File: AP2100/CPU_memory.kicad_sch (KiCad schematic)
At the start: 1 part, among them U3 LS1043ASE7KQB

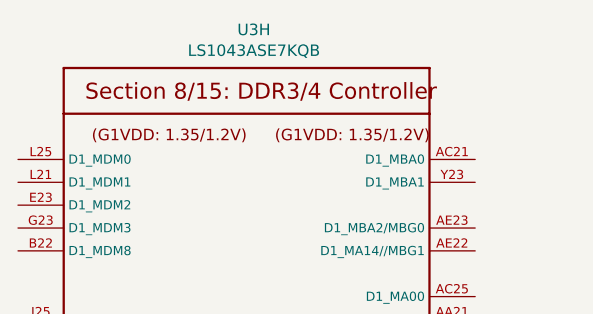
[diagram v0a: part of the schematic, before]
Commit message: Add PartsBox part numbers to everything so far
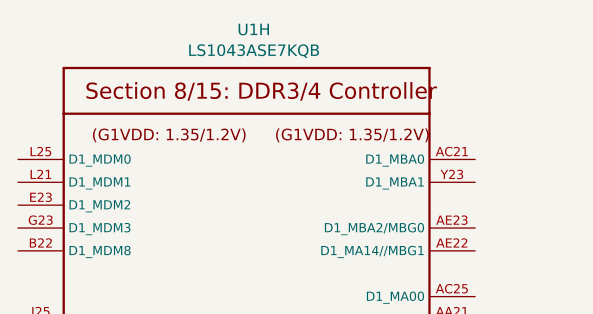
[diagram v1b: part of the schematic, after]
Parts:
- U1: renamed from U3; PartsBoxID (none) -> LS1043ASE7MNLB
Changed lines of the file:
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@@
   (symbol (lib_id "AP2100-rescue:LS1043ASE7KQB-Layerscape") (at 72.39 100.33 0) (unit 8)
     (in_bom yes) (on_board yes)
-    (property "Reference" "U3" (id 0) (at 71.9328 17.3482 0))
+    (property "Reference" "U1" (id 0) (at 71.9328 17.3482 0))
     (property "Value" "LS1043ASE7KQB" (id 1) (at 71.9328 19.6596 0))
     (property "Footprint" "PLS1043ASE7QQA:BGA621C80P25X25_2100X2100X192N" (id 2) (at 72.39 100.33 0)
@@
       (effects (font (size 1.27 1.27)) hide)
     )
+    (property "PartsBoxID" "LS1043ASE7MNLB" (id 4) (at 72.39 100.33 0)
+      (effects (font (size 1.27 1.27)) hide)
+    )

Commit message: More work on memory
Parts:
- added C? (x4): 1uF, Capacitor_SMD:C_0402_1005Metric, symbol Device:C_Small
- added C? (x16): .1uF, Capacitor_SMD:C_0402_1005Metric, symbol Device:C_Small
- added C? (x4): 10uF, Capacitor_SMD:C_0805_2012Metric, symbol Device:C_Small
- added IC3, IC4: AS4C256M16D4-75BCN, Scott:BGA96C80P9X16_750X1350X120, symbol Scott:AS4C256M16D4
- U1: MFR - -> (none)
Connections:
- new net +GVDD: C?.1, C?.1, C?.1, C?.1, C?.1, C?.1, C?.1, C?.1, C?.1, C?.1, C?.1, C?.1, C?.1, C?.1, C?.1, C?.1, C?.1, C?.1, C?.1, C?.1, IC3.A1 (VDDQ_1), IC3.A9 (VDDQ_2), IC3.B3 (VDD_1), IC3.B9 (VDD_2), IC3.C1 (VDDQ_3), IC3.D1 (VDD_3), IC3.D9 (VDDQ_4), IC3.F2 (VDDQ_5), IC3.F8 (VDDQ_6), IC3.G1 (VDDQ_7), IC3.G7 (VDD_4), IC3.G9 (VDDQ_8), IC3.J1 (VDD_5), IC3.J2 (VDDQ_9), IC3.J8 (VDDQ_10), IC3.J9 (VDD_6), IC3.L1 (VDD_7), IC3.L9 (VDD_8), IC3.R1 (VDD_9), IC3.T9 (VDD_10), IC4.A1 (VDDQ_1), IC4.A9 (VDDQ_2), IC4.B3 (VDD_1), IC4.B9 (VDD_2), IC4.C1 (VDDQ_3), IC4.D1 (VDD_3), IC4.D9 (VDDQ_4), IC4.F2 (VDDQ_5), IC4.F8 (VDDQ_6), IC4.G1 (VDDQ_7), IC4.G7 (VDD_4), IC4.G9 (VDDQ_8), IC4.J1 (VDD_5), IC4.J2 (VDDQ_9), IC4.J8 (VDDQ_10), IC4.J9 (VDD_6), IC4.L1 (VDD_7), IC4.L9 (VDD_8), IC4.R1 (VDD_9), IC4.T9 (VDD_10)
- new net 2V5_VPP: C?.1, C?.1, C?.1, C?.1, IC3.B1 (VPP_1), IC3.R9 (VPP_2), IC4.B1 (VPP_1), IC4.R9 (VPP_2)
- new net GND: C?.2, C?.2, C?.2, C?.2, C?.2, C?.2, C?.2, C?.2, C?.2, C?.2, C?.2, C?.2, C?.2, C?.2, C?.2, C?.2, C?.2, C?.2, C?.2, C?.2, C?.2, C?.2, C?.2, C?.2, IC3.A2 (VSSQ_1), IC3.A8 (VSSQ_2), IC3.B2 (VSS_1), IC3.C9 (VSSQ_3), IC3.D2 (VSSQ_4), IC3.D8 (VSSQ_5), IC3.E1 (VSS_2), IC3.E3 (VSSQ_6), IC3.E8 (VSSQ_7), IC3.E9 (VSS_3), IC3.F1 (VSSQ_8), IC3.G8 (VSS_4), IC3.H1 (VSSQ_9), IC3.H9 (VSSQ_10), IC3.K1 (VSS_5), IC3.K9 (VSS_6), IC3.M9 (VSS_7), IC3.N1 (VSS_8), IC3.T1 (VSS_9), IC4.A2 (VSSQ_1), IC4.A8 (VSSQ_2), IC4.B2 (VSS_1), IC4.C9 (VSSQ_3), IC4.D2 (VSSQ_4), IC4.D8 (VSSQ_5), IC4.E1 (VSS_2), IC4.E3 (VSSQ_6), IC4.E8 (VSSQ_7), IC4.E9 (VSS_3), IC4.F1 (VSSQ_8), IC4.G8 (VSS_4), IC4.H1 (VSSQ_9), IC4.H9 (VSSQ_10), IC4.K1 (VSS_5), IC4.K9 (VSS_6), IC4.M9 (VSS_7), IC4.N1 (VSS_8), IC4.T1 (VSS_9)
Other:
- moved on the sheet: U1H

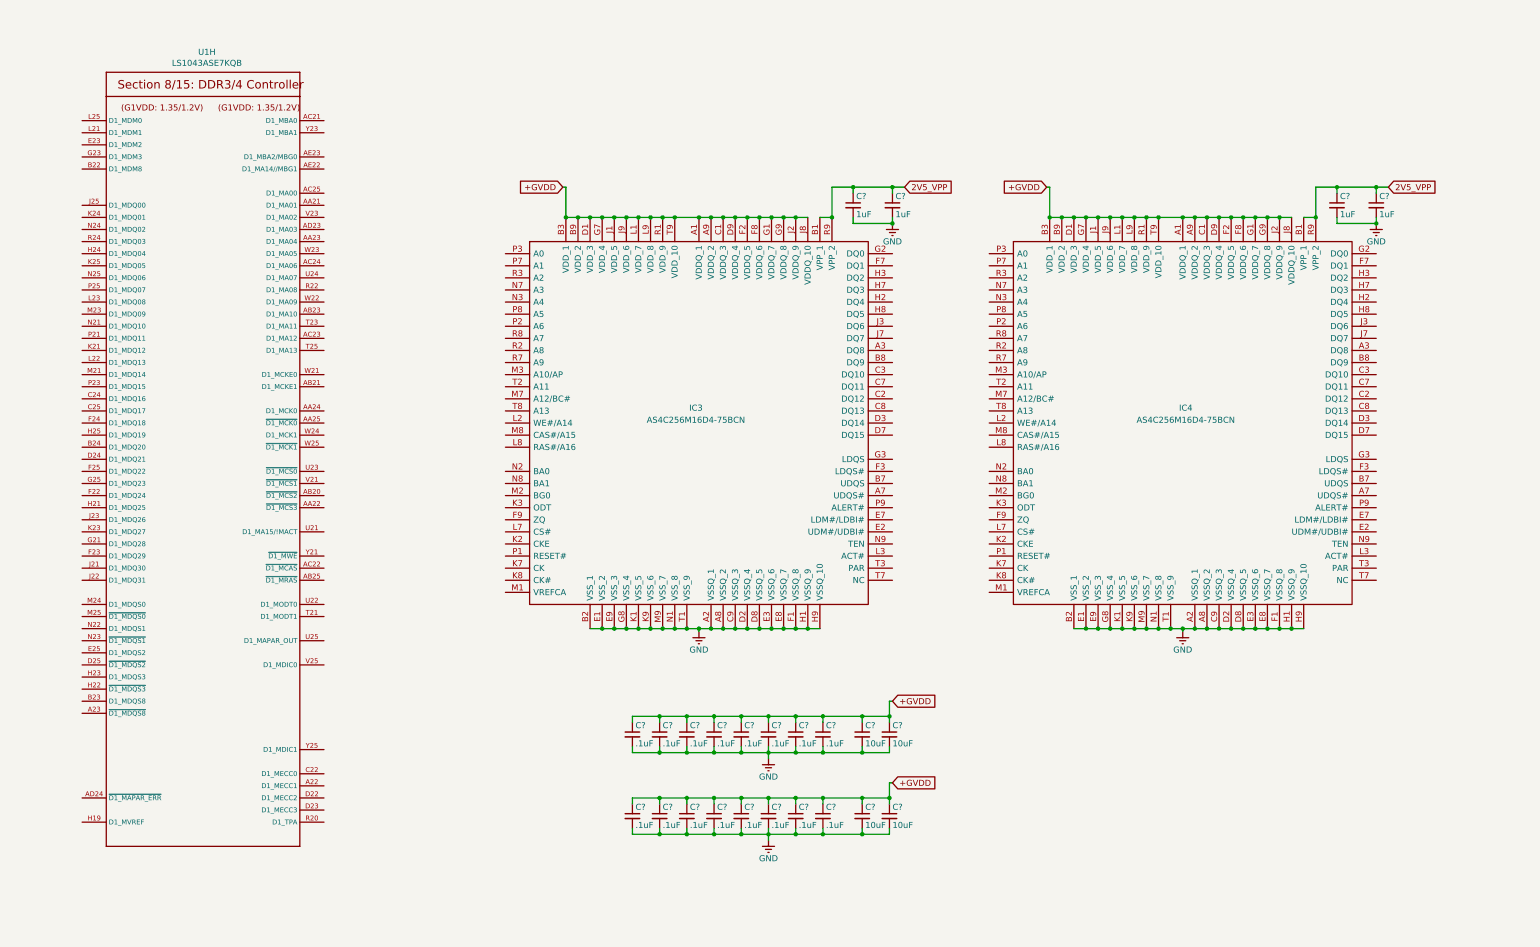
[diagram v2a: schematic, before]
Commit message: Add + route first 16 memory data lines
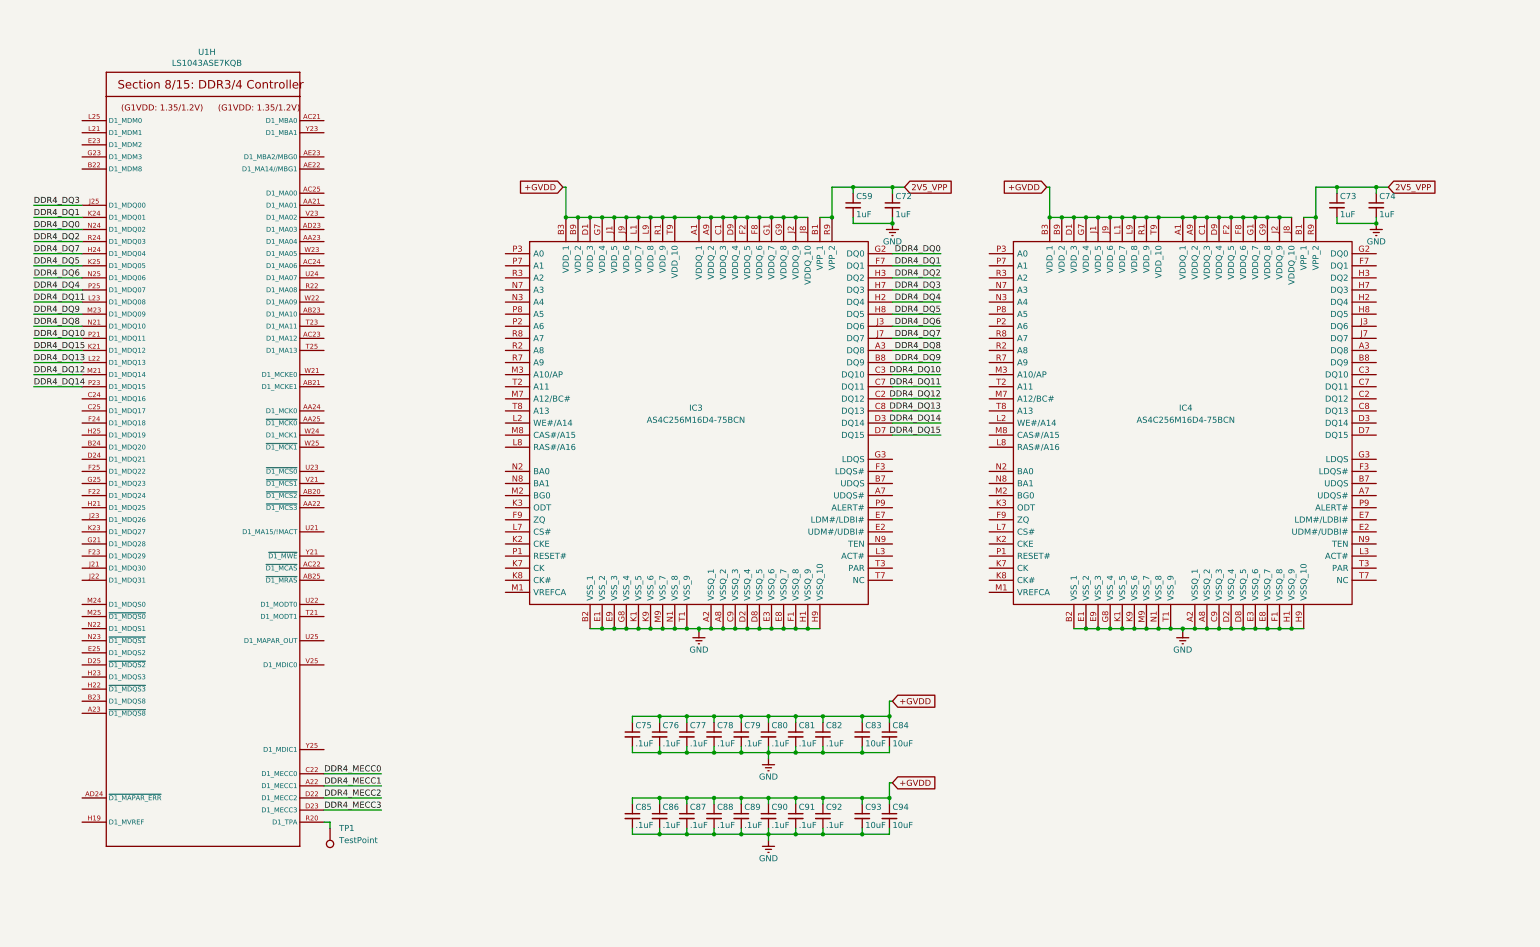
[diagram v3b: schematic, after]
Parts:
- added TP1: TestPoint, symbol Connector:TestPoint
- gave numbers to parts that had none: 24
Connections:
- net DDR4_MECC1: now reaches U1.A22 (D1_MECC1)
- net DDR4_MECC0: now reaches U1.C22 (D1_MECC0)
- net DDR4_MECC2: now reaches U1.D22 (D1_MECC2)
- net DDR4_MECC3: now reaches U1.D23 (D1_MECC3)
- net DDR4_DQ7: now reaches U1.H24 (D1_MDQ04)
- net DDR4_DQ7: now also IC3.J7 (DQ7)
- net DDR4_DQ3: now reaches U1.J25 (D1_MDQ00)
- net DDR4_DQ3: now also IC3.H7 (DQ3)
- net DDR4_DQ15: now reaches U1.K21 (D1_MDQ12)
- net DDR4_DQ15: now also IC3.D7 (DQ15)
- net DDR4_DQ1: now reaches U1.K24 (D1_MDQ01)
- net DDR4_DQ1: now also IC3.F7 (DQ1)
- net DDR4_DQ5: now reaches U1.K25 (D1_MDQ05)
- net DDR4_DQ5: now also IC3.H8 (DQ5)
- net DDR4_DQ13: now reaches U1.L22 (D1_MDQ13)
- net DDR4_DQ13: now also IC3.C8 (DQ13)
- net DDR4_DQ11: now reaches U1.L23 (D1_MDQ08)
- net DDR4_DQ11: now also IC3.C7 (DQ11)
- net DDR4_DQ12: now reaches U1.M21 (D1_MDQ14)
- net DDR4_DQ12: now also IC3.C2 (DQ12)
- net DDR4_DQ9: now reaches U1.M23 (D1_MDQ09)
- net DDR4_DQ9: now also IC3.B8 (DQ9)
- net DDR4_DQ8: now reaches U1.N21 (D1_MDQ10)
- net DDR4_DQ8: now also IC3.A3 (DQ8)
- net DDR4_DQ0: now reaches U1.N24 (D1_MDQ02)
- net DDR4_DQ0: now also IC3.G2 (DQ0)
- net DDR4_DQ6: now reaches U1.N25 (D1_MDQ06)
- net DDR4_DQ6: now also IC3.J3 (DQ6)
- net DDR4_DQ10: now reaches U1.P21 (D1_MDQ11)
- net DDR4_DQ10: now also IC3.C3 (DQ10)
- net DDR4_DQ14: now reaches U1.P23 (D1_MDQ15)
- net DDR4_DQ14: now also IC3.D3 (DQ14)
- net DDR4_DQ4: now reaches U1.P25 (D1_MDQ07)
- net DDR4_DQ4: now also IC3.H2 (DQ4)
- net at U1.R20 (D1_TPA): now also TP1.1
- net DDR4_DQ2: now reaches U1.R24 (D1_MDQ03)
- net DDR4_DQ2: now also IC3.H3 (DQ2)

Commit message: Almost finish memory section
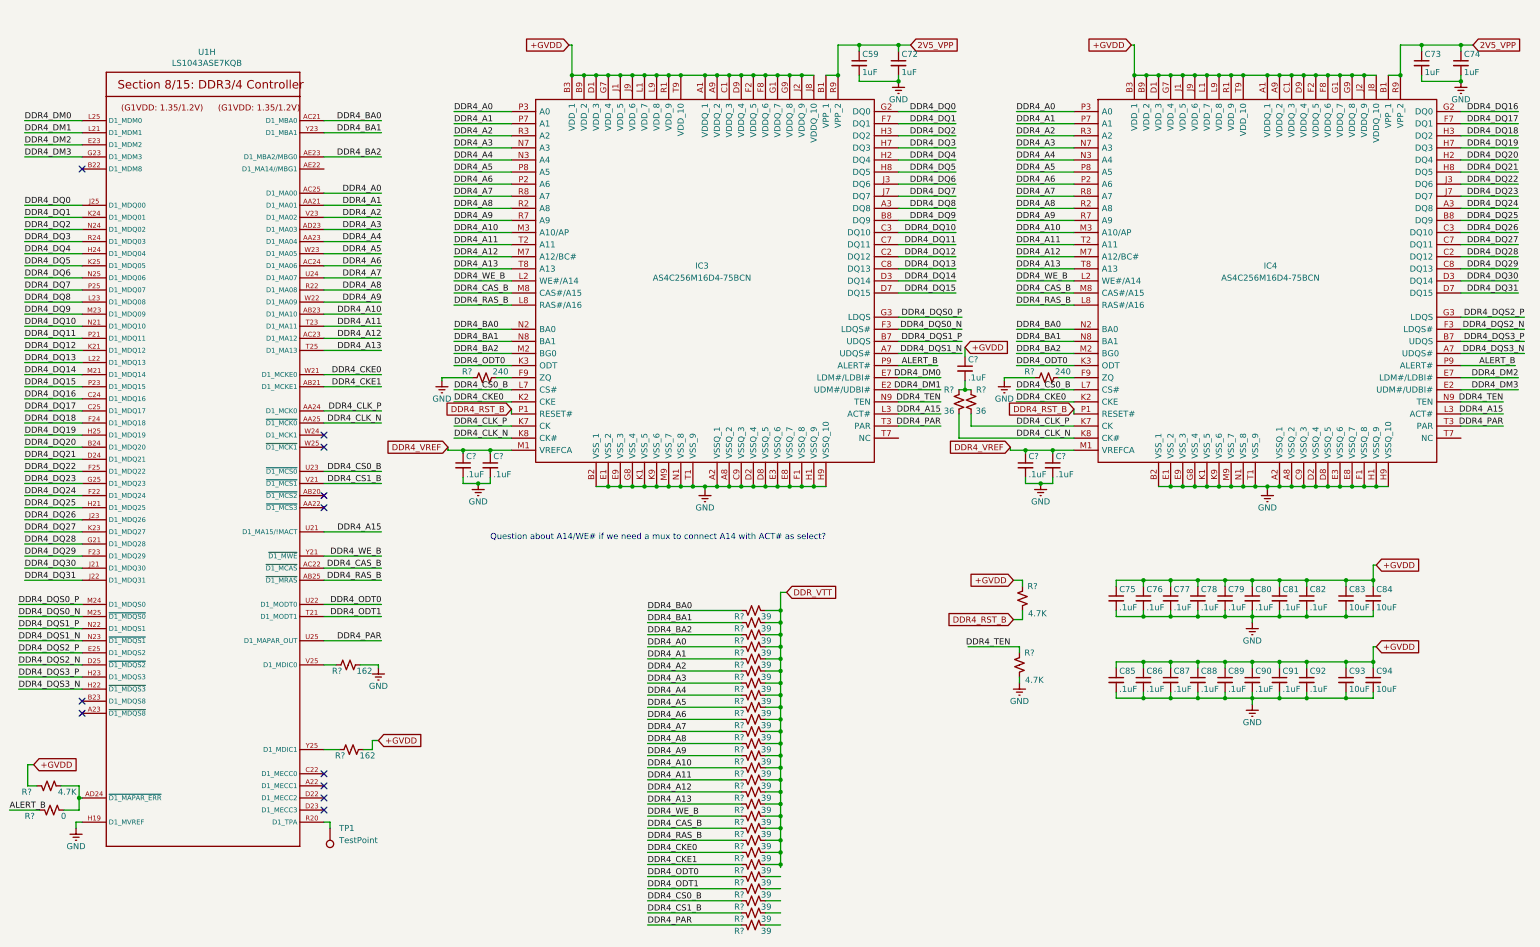
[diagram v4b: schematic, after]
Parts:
- added C? (x5): .1uF, Capacitor_SMD:C_0402_1005Metric, symbol Device:C_Small
- added R? (x27): 39, Resistor_SMD:R_0402_1005Metric, symbol Device:R_Small_US
- added R? (x2): 36, Resistor_SMD:R_0402_1005Metric, symbol Device:R_Small_US
- added R? (x2): 240, Resistor_SMD:R_0402_1005Metric, symbol Device:R_Small_US
- added R? (x3): 4.7K, Resistor_SMD:R_0402_1005Metric, symbol Device:R_Small_US
- added R?: 0, Resistor_SMD:R_0402_1005Metric, symbol Device:R_Small_US
- added R? (x2): 162, Resistor_SMD:R_0402_1005Metric, symbol Device:R_Small_US
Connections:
- net +GVDD: now also C?.1, R?.1, R?.2, R?.2
- net DDR4_DQ0: now also U1.J25 (D1_MDQ00); no longer U1.N24 (D1_MDQ02)
- net DDR4_DQ10: now also U1.N21 (D1_MDQ10); no longer U1.P21 (D1_MDQ11)
- net DDR4_DQ11: now also U1.P21 (D1_MDQ11); no longer U1.L23 (D1_MDQ08)
- net DDR4_DQ12: now also U1.K21 (D1_MDQ12); no longer U1.M21 (D1_MDQ14)
- net DDR4_DQ14: now also U1.M21 (D1_MDQ14); no longer U1.P23 (D1_MDQ15)
- net DDR4_DQ15: now also U1.P23 (D1_MDQ15); no longer U1.K21 (D1_MDQ12)
- net DDR4_DQ2: now also U1.N24 (D1_MDQ02); no longer U1.R24 (D1_MDQ03)
- net DDR4_DQ3: now also U1.R24 (D1_MDQ03); no longer U1.J25 (D1_MDQ00)
- net DDR4_DQ4: now also U1.H24 (D1_MDQ04); no longer U1.P25 (D1_MDQ07)
- net DDR4_DQ7: now also U1.P25 (D1_MDQ07); no longer U1.H24 (D1_MDQ04)
- net DDR4_DQ8: now also U1.L23 (D1_MDQ08); no longer U1.N21 (D1_MDQ10)
- net GND: now also U1.H19 (D1_MVREF), C?.2, C?.2, C?.2, C?.2, R?.1, R?.1, R?.2, R?.2
- net DDR4_A1: now reaches U1.AA21 (D1_MA01)
- net DDR4_A1: now also IC3.P7 (A1), IC4.P7 (A1), R?.1
- net DDR4_A4: now reaches U1.AA23 (D1_MA04)
- net DDR4_A4: now also IC3.N3 (A4), IC4.N3 (A4), R?.1
- net DDR4_CLK_P: now reaches U1.AA24 (D1_MCK0)
- net DDR4_CLK_P: now also IC3.K7 (CK), IC4.K7 (CK), R?.1
- net DDR4_CLK_N: now reaches U1.AA25 (~D1_MCK0~)
- net DDR4_CLK_N: now also IC3.K8 (CK#), IC4.K8 (CK#), R?.1
- net DDR4_CKE1: now reaches U1.AB21 (D1_MCKE1)
- net DDR4_CKE1: now also R?.1
- net DDR4_A10: now reaches U1.AB23 (D1_MA10)
- net DDR4_A10: now also IC3.M3 (A10/AP), IC4.M3 (A10/AP), R?.1
- net DDR4_RAS_B: now reaches U1.AB25 (~D1_MRAS~)
- net DDR4_RAS_B: now also IC3.L8 (RAS#/A16), IC4.L8 (RAS#/A16), R?.1
- net DDR4_BA0: now reaches U1.AC21 (D1_MBA0)
- net DDR4_BA0: now also IC3.N2 (BA0), IC4.N2 (BA0), R?.1
- net DDR4_CAS_B: now reaches U1.AC22 (~D1_MCAS~)
- net DDR4_CAS_B: now also IC3.M8 (CAS#/A15), IC4.M8 (CAS#/A15), R?.1
- net DDR4_A12: now reaches U1.AC23 (D1_MA12)
- net DDR4_A12: now also IC3.M7 (A12/BC#), IC4.M7 (A12/BC#), R?.1
- net DDR4_A6: now reaches U1.AC24 (D1_MA06)
- net DDR4_A6: now also IC3.P2 (A6), IC4.P2 (A6), R?.1
- net DDR4_A0: now reaches U1.AC25 (D1_MA00)
- net DDR4_A0: now also IC3.P3 (A0), IC4.P3 (A0), R?.1
- net DDR4_A3: now reaches U1.AD23 (D1_MA03)
- net DDR4_A3: now also IC3.N7 (A3), IC4.N7 (A3), R?.1
- net at U1.AD24 (~D1_MAPAR_ERR~): now also R?.1, R?.1
- net DDR4_BA2: now reaches U1.AE23 (D1_MBA2/MBG0)
- net DDR4_BA2: now also IC3.M2 (BG0), IC4.M2 (BG0), R?.1
- net DDR4_DQ20: now reaches U1.B24 (D1_MDQ20)
- net DDR4_DQ20: now also IC4.H2 (DQ4)
- net DDR4_DQ16: now reaches U1.C24 (D1_MDQ16)
- net DDR4_DQ16: now also IC4.G2 (DQ0)
- net DDR4_DQ17: now reaches U1.C25 (D1_MDQ17)
- net DDR4_DQ17: now also IC4.F7 (DQ1)
- net DDR4_DQ21: now reaches U1.D24 (D1_MDQ21)
- net DDR4_DQ21: now also IC4.H8 (DQ5)
- net DDR4_DQS2_N: now reaches U1.D25 (~D1_MDQS2~)
- net DDR4_DQS2_N: now also IC4.F3 (LDQS#)
- net DDR4_DM2: now reaches U1.E23 (D1_MDM2)
- net DDR4_DM2: now also IC4.E7 (LDM#/LDBI#)
- net DDR4_DQS2_P: now reaches U1.E25 (D1_MDQS2)
- net DDR4_DQS2_P: now also IC4.G3 (LDQS)
- net DDR4_DQ24: now reaches U1.F22 (D1_MDQ24)
- net DDR4_DQ24: now also IC4.A3 (DQ8)
- net DDR4_DQ29: now reaches U1.F23 (D1_MDQ29)
- net DDR4_DQ29: now also IC4.C8 (DQ13)
- net DDR4_DQ18: now reaches U1.F24 (D1_MDQ18)
- net DDR4_DQ18: now also IC4.H3 (DQ2)
- net DDR4_DQ22: now reaches U1.F25 (D1_MDQ22)
- net DDR4_DQ22: now also IC4.J3 (DQ6)
- net DDR4_DQ28: now reaches U1.G21 (D1_MDQ28)
- net DDR4_DQ28: now also IC4.C2 (DQ12)
- net DDR4_DM3: now reaches U1.G23 (D1_MDM3)
- net DDR4_DM3: now also IC4.E2 (UDM#/UDBI#)
- net DDR4_DQ23: now reaches U1.G25 (D1_MDQ23)
- net DDR4_DQ23: now also IC4.J7 (DQ7)
- net DDR4_DQ25: now reaches U1.H21 (D1_MDQ25)
- net DDR4_DQ25: now also IC4.B8 (DQ9)
- net DDR4_DQS3_N: now reaches U1.H22 (~D1_MDQS3~)
- net DDR4_DQS3_N: now also IC4.A7 (UDQS#)
- net DDR4_DQS3_P: now reaches U1.H23 (D1_MDQS3)
- net DDR4_DQS3_P: now also IC4.B7 (UDQS)
- net DDR4_DQ19: now reaches U1.H25 (D1_MDQ19)
- net DDR4_DQ19: now also IC4.H7 (DQ3)
- net DDR4_DQ30: now reaches U1.J21 (D1_MDQ30)
- net DDR4_DQ30: now also IC4.D3 (DQ14)
- net DDR4_DQ31: now reaches U1.J22 (D1_MDQ31)
- net DDR4_DQ31: now also IC4.D7 (DQ15)
- net DDR4_DQ26: now reaches U1.J23 (D1_MDQ26)
- net DDR4_DQ26: now also IC4.C3 (DQ10)
- net DDR4_DQ27: now reaches U1.K23 (D1_MDQ27)
- net DDR4_DQ27: now also IC4.C7 (DQ11)
- net DDR4_DM1: now reaches U1.L21 (D1_MDM1)
- net DDR4_DM1: now also IC3.E2 (UDM#/UDBI#)
- net DDR4_DM0: now reaches U1.L25 (D1_MDM0)
- net DDR4_DM0: now also IC3.E7 (LDM#/LDBI#)
- net DDR4_DQS0_P: now reaches U1.M24 (D1_MDQS0)
- net DDR4_DQS0_P: now also IC3.G3 (LDQS)
- net DDR4_DQS0_N: now reaches U1.M25 (~D1_MDQS0~)
- net DDR4_DQS0_N: now also IC3.F3 (LDQS#)
- net DDR4_DQS1_P: now reaches U1.N22 (D1_MDQS1)
- net DDR4_DQS1_P: now also IC3.B7 (UDQS)
- net DDR4_DQS1_N: now reaches U1.N23 (~D1_MDQS1~)
- net DDR4_DQS1_N: now also IC3.A7 (UDQS#)
- net DDR4_A8: now reaches U1.R22 (D1_MA08)
- net DDR4_A8: now also IC3.R2 (A8), IC4.R2 (A8), R?.1
- net DDR4_ODT1: now reaches U1.T21 (D1_MODT1)
- net DDR4_ODT1: now also R?.1
- net DDR4_A11: now reaches U1.T23 (D1_MA11)
- net DDR4_A11: now also IC3.T2 (A11), IC4.T2 (A11), R?.1
- net DDR4_A13: now reaches U1.T25 (D1_MA13)
- net DDR4_A13: now also IC3.T8 (A13), IC4.T8 (A13), R?.1
- net DDR4_A15: now reaches U1.U21 (D1_MA15/!MACT)
- net DDR4_A15: now also IC3.L3 (ACT#), IC4.L3 (ACT#)
- net DDR4_ODT0: now reaches U1.U22 (D1_MODT0)
- net DDR4_ODT0: now also IC3.K3 (ODT), IC4.K3 (ODT), R?.1
- net DDR4_CS0_B: now reaches U1.U23 (~D1_MCS0~)
- net DDR4_CS0_B: now also IC3.L7 (CS#), IC4.L7 (CS#), R?.1
- net DDR4_A7: now reaches U1.U24 (D1_MA07)
- net DDR4_A7: now also IC3.R8 (A7), IC4.R8 (A7), R?.1
- net DDR4_PAR: now reaches U1.U25 (D1_MAPAR_OUT)
- net DDR4_PAR: now also IC3.T3 (PAR), IC4.T3 (PAR), R?.1
- net DDR4_CS1_B: now reaches U1.V21 (~D1_MCS1~)
- net DDR4_CS1_B: now also R?.1
- net DDR4_A2: now reaches U1.V23 (D1_MA02)
- net DDR4_A2: now also IC3.R3 (A2), IC4.R3 (A2), R?.1
- net at U1.V25 (D1_MDIC0): now also R?.1
- net DDR4_CKE0: now reaches U1.W21 (D1_MCKE0)
- net DDR4_CKE0: now also IC3.K2 (CKE), IC4.K2 (CKE), R?.1
- net DDR4_A9: now reaches U1.W22 (D1_MA09)
- net DDR4_A9: now also IC3.R7 (A9), IC4.R7 (A9), R?.1
- net DDR4_A5: now reaches U1.W23 (D1_MA05)
- net DDR4_A5: now also IC3.P8 (A5), IC4.P8 (A5), R?.1
- net DDR4_WE_B: now reaches U1.Y21 (~D1_MWE~)
- net DDR4_WE_B: now also IC3.L2 (WE#/A14), IC4.L2 (WE#/A14), R?.1
- net DDR4_BA1: now reaches U1.Y23 (D1_MBA1)
- net DDR4_BA1: now also IC3.N8 (BA1), IC4.N8 (BA1), R?.1
- net at U1.Y25 (D1_MDIC1): now also R?.1
- net at IC4.F9 (ZQ): now also R?.2
- net DDR4_VREF: now reaches IC4.M1 (VREFCA)
- net DDR4_VREF: now also IC3.M1 (VREFCA), C?.1, C?.1, C?.1, C?.1
- net DDR4_TEN: now reaches IC4.N9 (TEN)
- net DDR4_TEN: now also IC3.N9 (TEN), R?.1
- net DDR4_RST_B: now reaches IC4.P1 (RESET#)
- net DDR4_RST_B: now also IC3.P1 (RESET#), R?.2
- net ALERT_B: now reaches IC4.P9 (ALERT#)
- net ALERT_B: now also IC3.P9 (ALERT#), R?.2
- net at IC3.F9 (ZQ): now also R?.2
- net DDR4_MECC0: no longer names the net of U1.C22 (D1_MECC0)
- net DDR4_MECC1: no longer names the net of U1.A22 (D1_MECC1)
- net DDR4_MECC2: no longer names the net of U1.D22 (D1_MECC2)
- net DDR4_MECC3: no longer names the net of U1.D23 (D1_MECC3)
- new net: C?.2, R?.2, R?.2
- new net DDR_VTT: R?.2, R?.2, R?.2, R?.2, R?.2, R?.2, R?.2, R?.2, R?.2, R?.2, R?.2, R?.2, R?.2, R?.2, R?.2, R?.2, R?.2, R?.2, R?.2, R?.2, R?.2, R?.2
- no-connect marks 0 -> 11
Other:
- note added: "Question about A14/WE# if we need a mux to connect A14 with ACT# as select?"
- moved on the sheet: C59, C72, C73, C74, C75, C76, C77, C78, C79, C80, C81, C82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

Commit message: Finalize DDR4 memory section
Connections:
- no-connect marks 11 -> 12
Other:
- note removed: "Question about A14/WE# if we need a mux to connect A14 with ACT# as select?"
- moved on the sheet: R?

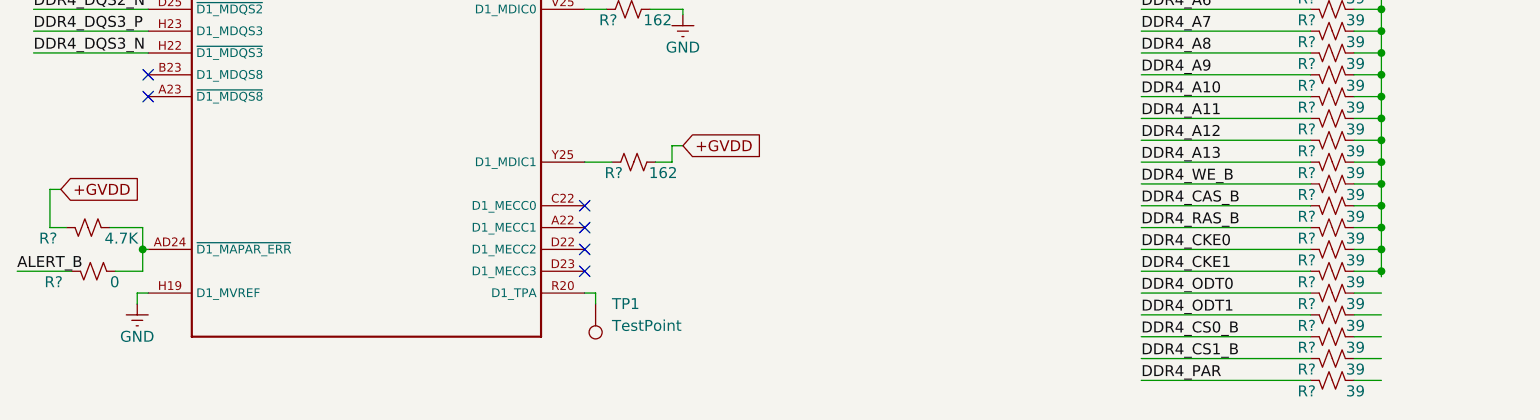
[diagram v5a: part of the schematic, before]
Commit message: Add emmc library part but likely will delete
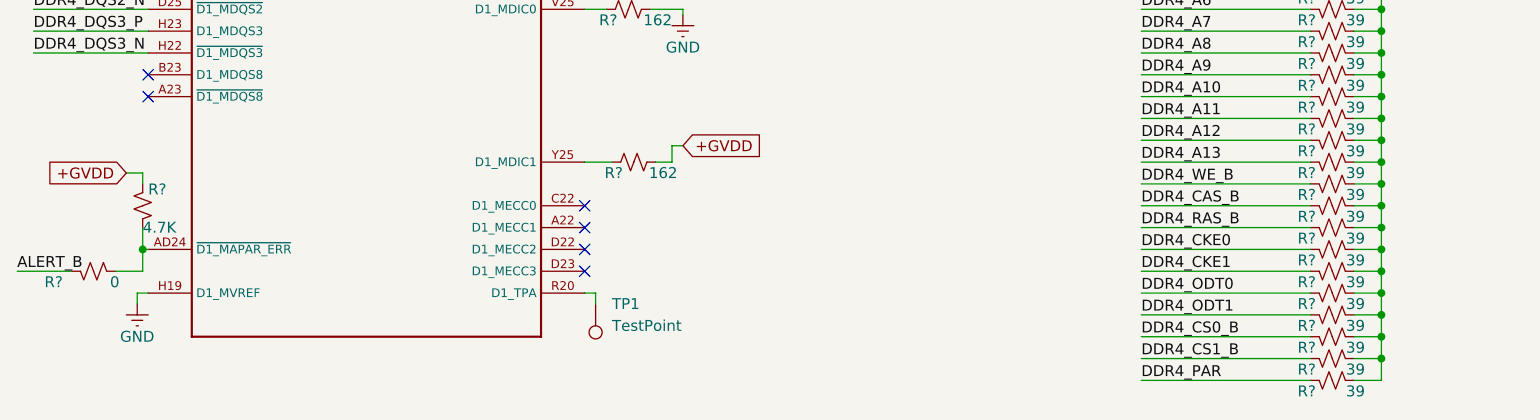
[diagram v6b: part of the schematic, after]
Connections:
- net DDR_VTT: now also R?.2, R?.2, R?.2, R?.2, R?.2
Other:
- moved on the sheet: R?
